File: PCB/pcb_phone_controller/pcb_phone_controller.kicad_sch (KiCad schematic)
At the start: 38 parts, among them SW17 SS-12D00-G 4 E, X1 KAILH-MINI-SILENT-SWITCH, Y1 KAILH-MINI-SILENT-SWITCH

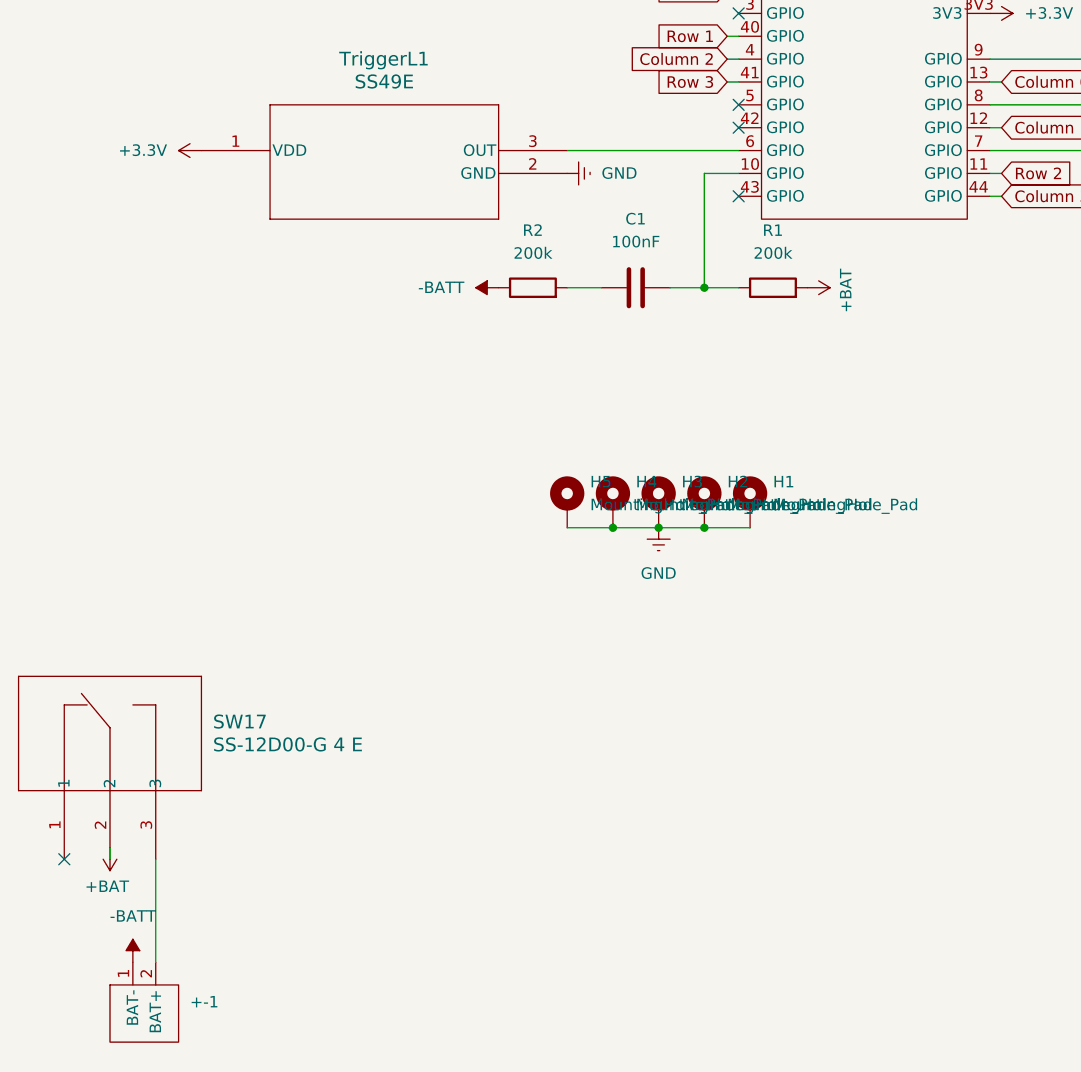
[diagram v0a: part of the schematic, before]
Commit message: Add pads to connect the battery to the µcontroller + add assembly guide
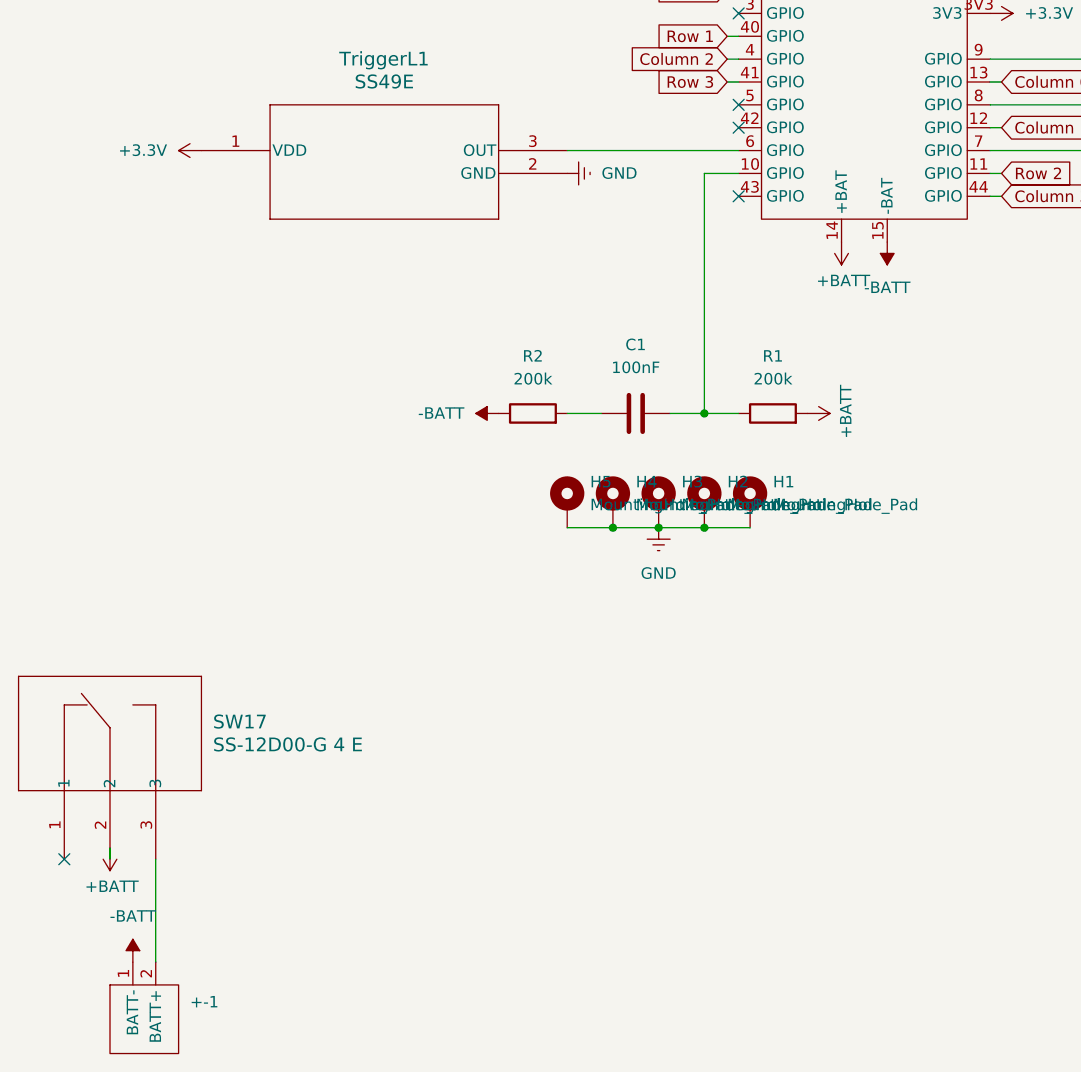
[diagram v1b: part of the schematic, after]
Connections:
- net -BATT: now also U1.15 (-BAT)
- net +BAT renamed +BATT
- net +BATT: now also U1.14 (+BAT)
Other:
- moved on the sheet: +-1, C1, R1, R2
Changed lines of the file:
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@@
 	)
 	(junction
-		(at 109.22 83.82)
+		(at 109.22 97.79)
 		(diameter 0)
 		(color 0 0 0 0)
@@
 	(wire
 		(pts
-			(xy 109.22 71.12) (xy 109.22 83.82)
+			(xy 109.22 71.12) (xy 109.22 97.79)
 		)
 		(stroke
@@
 	(wire
 		(pts
-			(xy 105.41 83.82) (xy 109.22 83.82)
+			(xy 105.41 97.79) (xy 109.22 97.79)
 		)
 		(stroke
@@
 	(wire
 		(pts
-			(xy 93.98 83.82) (xy 97.79 83.82)
+			(xy 93.98 97.79) (xy 97.79 97.79)
 		)
 		(stroke
@@
 	(wire
 		(pts
-			(xy 113.03 83.82) (xy 109.22 83.82)
+			(xy 113.03 97.79) (xy 109.22 97.79)
 		)
 		(stroke
@@
 		(pin "13"
 		)
+		(pin "15"
+		)
+		(pin "14"
+		)
 		(instances
 			(project ""
@@
 	)
 	(symbol
+		(lib_id "power:-BATT")
+		(at 129.54 78.74 180)
+		(unit 1)
+		(exclude_from_sim no)
+		(in_bom yes)
+		(on_board yes)
+		(dnp no)
+		(property "Reference" "#PWR013"
+			(at 129.54 74.93 0)
+			(effects
+				(font
+					(size 1.27 1.27)
+				)
+				(hide yes)
+			)
+		)
+		(property "Value" "-BATT"
+			(at 129.54 83.82 0)
+			(effects
+				(font
+					(size 1.27 1.27)
+				)
+			)
+		)
+		(property "Footprint" ""
+			(at 129.54 78.74 0)
+			(effects
+				(font
+					(size 1.27 1.27)
+				)
+				(hide yes)
+			)
+		)
+		(property "Datasheet" ""
+			(at 129.54 78.74 0)
+			(effects
+				(font
+					(size 1.27 1.27)
+				)
+				(hide yes)
+			)
+		)
+		(property "Description" "Power symbol creates a global label with name \"-BATT\""
+			(at 129.54 78.74 0)
+			(effects
+				(font
+					(size 1.27 1.27)
+				)
+				(hide yes)
+			)
+		)
+		(pin "1"
+		)
+		(instances
+			(project "pcb_phone_controller"
+				(path "/fc840a9c-b1ba-43df-b29f-5e3875a3bf9d"
+					(reference "#PWR013")
+					(unit 1)
+				)
+			)
+		)
+	)
+	(symbol
 		(lib_id "power:Earth")
 		(at 255.27 115.57 0)
@@
 	(symbol
 		(lib_id "Device:C")
-		(at 101.6 83.82 270)
+		(at 101.6 97.79 270)
 		(unit 1)
 		(exclude_from_sim no)
@@
 		(fields_autoplaced yes)
 		(property "Reference" "C1"
-			(at 101.6 76.2 90)
+			(at 101.6 90.17 90)
 			(effects
 				(font
@@
 		)
 		(property "Value" "100nF"
-			(at 101.6 78.74 90)
+			(at 101.6 92.71 90)
 			(effects
 				(font
@@
 		)
 		(property "Footprint" "Capacitor_SMD:C_0805_2012Metric_Pad1.18x1.45mm_HandSolder"
-			(at 97.79 84.7852 0)
+			(at 97.79 98.7552 0)
 			(effects
 				(font
@@
 		)
 		(property "Datasheet" "~"
-			(at 101.6 83.82 0)
+			(at 101.6 97.79 0)
 			(effects
 				(font
@@
 		)
 		(property "Description" "Unpolarized capacitor"
-			(at 101.6 83.82 0)
+			(at 101.6 97.79 0)
 			(effects
 				(font
@@
 	(symbol
 		(lib_id "power:+BATT")
-		(at 120.65 83.82 270)
+		(at 120.65 97.79 270)
 		(unit 1)
 		(exclude_from_sim no)
@@
 		(dnp no)
 		(property "Reference" "#PWR04"
-			(at 116.84 83.82 0)
+			(at 116.84 97.79 0)
 			(effects
 				(font
@@
 			)
 		)
-		(property "Value" "+BAT"
-			(at 124.968 86.614 0)
+		(property "Value" "+BATT"
+			(at 124.968 100.584 0)
 			(effects
 				(font
@@
 		)
 		(property "Footprint" ""
-			(at 120.65 83.82 0)
+			(at 120.65 97.79 0)
 			(effects
 				(font
@@
 		)
 		(property "Datasheet" ""
-			(at 120.65 83.82 0)
+			(at 120.65 97.79 0)
 			(effects
 				(font
@@
 		)
 		(property "Description" "Power symbol creates a global label with name \"+BATT\""
-			(at 120.65 83.82 0)
+			(at 120.65 97.79 0)
 			(effects
 				(font
@@
 			)
 		)
-		(property "Value" "+BAT"
+		(property "Value" "+BATT"
 			(at 40.386 150.368 0)
 			(effects
@@
 	(symbol
 		(lib_id "Device:R")
-		(at 90.17 83.82 90)
+		(at 90.17 97.79 90)
 		(unit 1)
 		(exclude_from_sim no)
@@
 		(fields_autoplaced yes)
 		(property "Reference" "R2"
-			(at 90.17 77.47 90)
+			(at 90.17 91.44 90)
 			(effects
 				(font
@@
 		)
 		(property "Value" "200k"
-			(at 90.17 80.01 90)
+			(at 90.17 93.98 90)
 			(effects
 				(font
@@
 		)
 		(property "Footprint" "Resistor_SMD:R_0805_2012Metric_Pad1.20x1.40mm_HandSolder"
-			(at 90.17 85.598 90)
+			(at 90.17 99.568 90)
 			(effects
 				(font
@@
 		)
 		(property "Datasheet" "~"
-			(at 90.17 83.82 0)
+			(at 90.17 97.79 0)
 			(effects
 				(font
@@
 		)
 		(property "Description" "Resistor"
-			(at 90.17 83.82 0)
+			(at 90.17 97.79 0)
 			(effects
 				(font
@@
 	(symbol
 		(lib_id "Device:R")
-		(at 116.84 83.82 90)
+		(at 116.84 97.79 90)
 		(unit 1)
 		(exclude_from_sim no)
@@
 		(fields_autoplaced yes)
 		(property "Reference" "R1"
-			(at 116.84 77.47 90)
+			(at 116.84 91.44 90)
 			(effects
 				(font
@@
 		)
 		(property "Value" "200k"
-			(at 116.84 80.01 90)
+			(at 116.84 93.98 90)
 			(effects
 				(font
@@
 		)
 		(property "Footprint" "Resistor_SMD:R_0805_2012Metric_Pad1.20x1.40mm_HandSolder"
-			(at 116.84 85.598 90)
+			(at 116.84 99.568 90)
 			(effects
 				(font
@@
 		)
 		(property "Datasheet" "~"
-			(at 116.84 83.82 0)
+			(at 116.84 97.79 0)
 			(effects
 				(font
@@
 		)
 		(property "Description" "Resistor"
-			(at 116.84 83.82 0)
+			(at 116.84 97.79 0)
 			(effects
 				(font
@@
 	(symbol
 		(lib_id "power:-BATT")
-		(at 86.36 83.82 90)
+		(at 86.36 97.79 90)
 		(unit 1)
 		(exclude_from_sim no)
@@
 		(fields_autoplaced yes)
 		(property "Reference" "#PWR05"
-			(at 90.17 83.82 0)
+			(at 90.17 97.79 0)
 			(effects
 				(font
@@
 		)
 		(property "Value" "-BATT"
-			(at 82.55 83.8199 90)
+			(at 82.55 97.7899 90)
 			(effects
 				(font
@@
 		)
 		(property "Footprint" ""
-			(at 86.36 83.82 0)
+			(at 86.36 97.79 0)
 			(effects
 				(font
@@
 		)
 		(property "Datasheet" ""
-			(at 86.36 83.82 0)
+			(at 86.36 97.79 0)
 			(effects
 				(font
@@
 			)
 		)
-		(property "Description" "Power symbol creates a global label with name \"-BATT\""
-			(at 86.36 83.82 0)
+		(property "Description" "Power symbol creates a global label with name \"-BAT\""
+			(at 86.36 97.79 0)
+			(effects
+				(font
+					(size 1.27 1.27)
+				)
+				(hide yes)
+			)
+		)
+		(property "Field5" ""
+			(at 86.36 97.79 0)
 			(effects
 				(font
@@
 					(unit 1)
 				)
+			)
+		)
+	)
+	(symbol
+		(lib_id "power:+BATT")
+		(at 124.46 78.74 180)
+		(unit 1)
+		(exclude_from_sim no)
+		(in_bom yes)
+		(on_board yes)
+		(dnp no)
+		(property "Reference" "#PWR03"
+			(at 124.46 74.93 0)
+			(effects
+				(font
+					(size 1.27 1.27)
+				)
+				(hide yes)
+			)
+		)
+		(property "Value" "+BATT"
+			(at 121.666 83.058 0)
+			(effects
+				(font
+					(size 1.27 1.27)
+				)
+				(justify right)
+			)
+		)
+		(property "Footprint" ""
+			(at 124.46 78.74 0)
+			(effects
+				(font
+					(size 1.27 1.27)
+				)
+				(hide yes)
+			)
+		)
+		(property "Datasheet" ""
+			(at 124.46 78.74 0)
+			(effects
+				(font
+					(size 1.27 1.27)
+				)
+				(hide yes)
+			)
+		)
+		(property "Description" "Power symbol creates a global label with name \"+BATT\""
+			(at 124.46 78.74 0)
+			(effects
+				(font
+					(size 1.27 1.27)
+				)
+				(hide yes)
+			)
+		)
+		(pin "1"
+		)
+		(instances
+			(project "pcb_phone_controller"
+				(path "/fc840a9c-b1ba-43df-b29f-5e3875a3bf9d"
+					(reference "#PWR03")
+					(unit 1)
+				)

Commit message: Add a 3D model for the TTP223
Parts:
- BumperL1, BumperR1, ClickStickL1, ClickStickR1: footprint Lib_controller:PinHeader_1x03_P2.54mm_Vertical -> Lib_controller:TTP223
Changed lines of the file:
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@@
 			)
 		)
-		(property "Footprint" "Lib_controller:PinHeader_1x03_P2.54mm_Vertical"
+		(property "Footprint" "Lib_controller:TTP223"
 			(at 213.36 105.41 0)
 			(effects
@@
 			)
 		)
-		(property "Footprint" "Lib_controller:PinHeader_1x03_P2.54mm_Vertical"
+		(property "Footprint" "Lib_controller:TTP223"
 			(at 236.22 105.41 0)
 			(effects
@@
 			)
 		)
-		(property "Footprint" "Lib_controller:PinHeader_1x03_P2.54mm_Vertical"
+		(property "Footprint" "Lib_controller:TTP223"
 			(at 252.73 105.41 0)
 			(effects
@@
 			)
 		)
-		(property "Footprint" "Lib_controller:PinHeader_1x03_P2.54mm_Vertical"
+		(property "Footprint" "Lib_controller:TTP223"
 			(at 275.59 105.41 0)
 			(effects

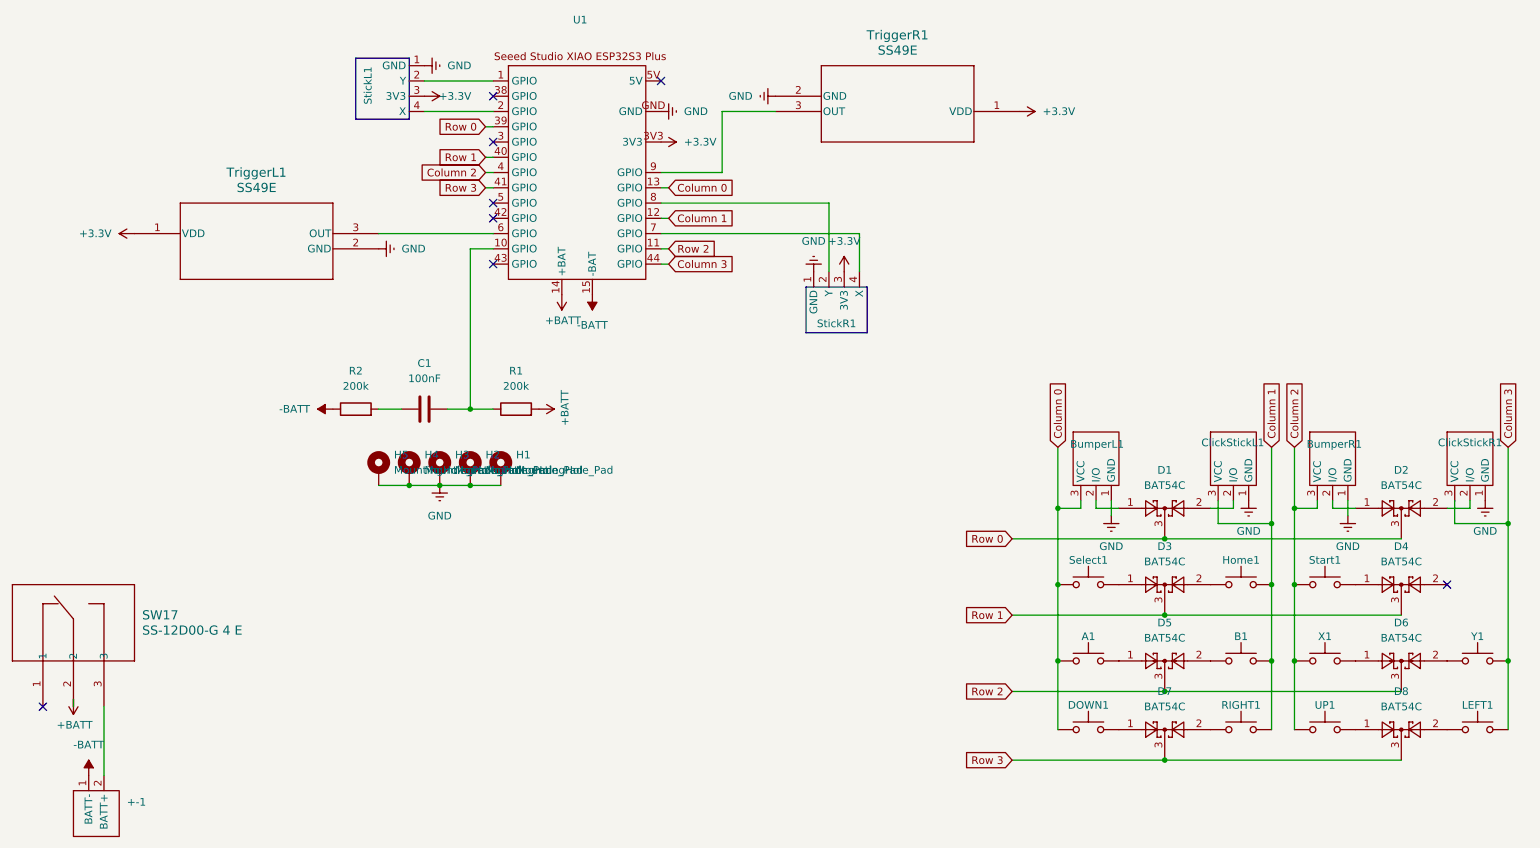
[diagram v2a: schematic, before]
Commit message: Change capacitives buttons to digitals ones and add real pullup
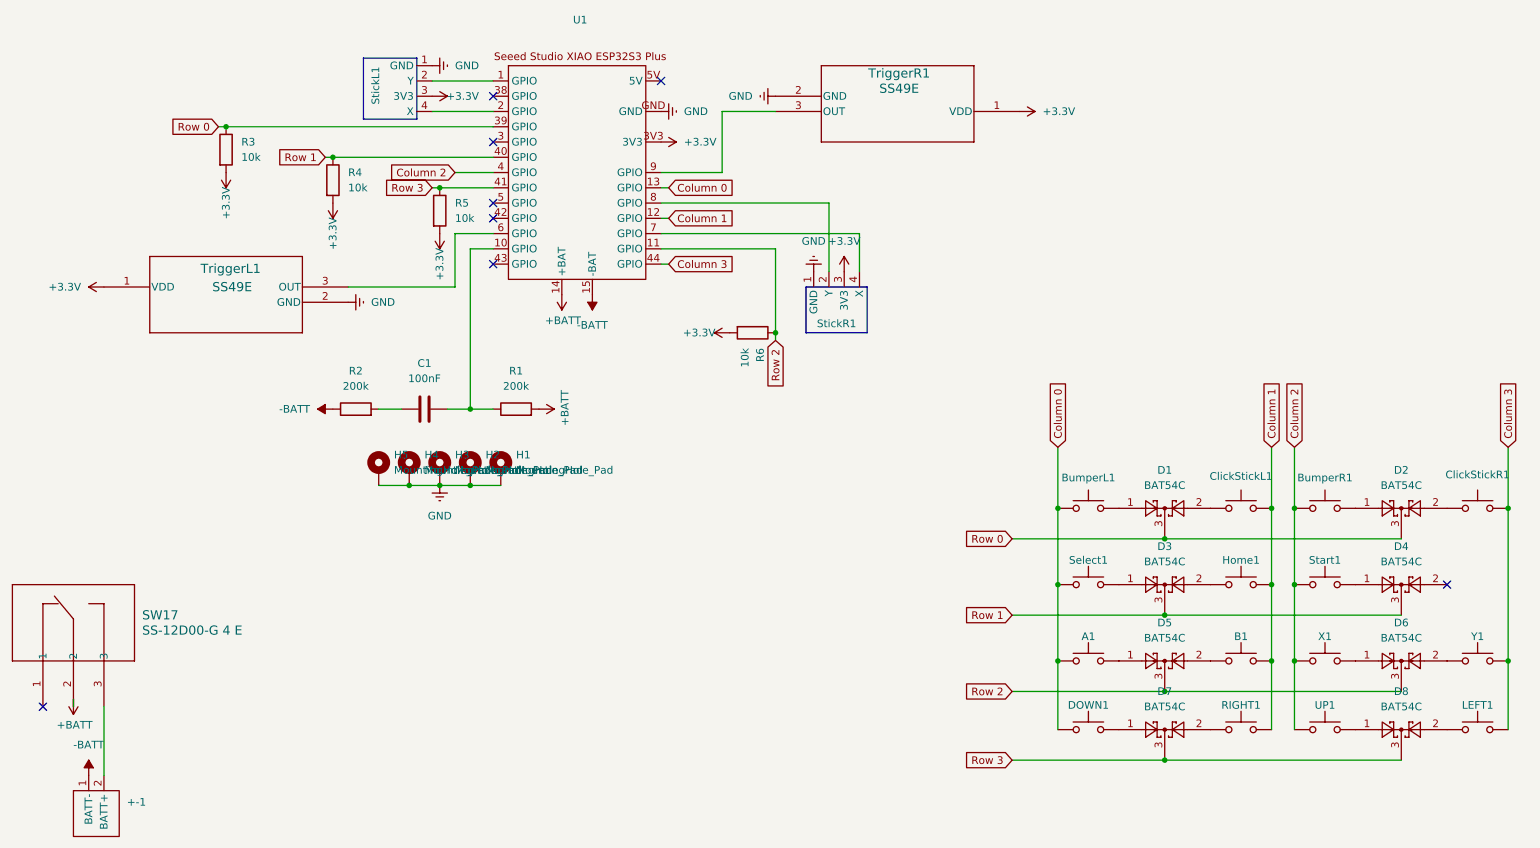
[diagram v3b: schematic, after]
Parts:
- removed BumperL1, BumperR1, ClickStickL1, ClickStickR1: ~, Lib_controller:TTP223, symbol Lib_controller:Capacitive_touch_sensor
- added BumperL1, BumperR1, ClickStickL1, ClickStickR1: Thin membrane button, Lib_controller:SKRWADE030, symbol Lib_controller:Membrane_button
- added R3, R4, R5, R6: 10k, Resistor_SMD:R_0805_2012Metric_Pad1.20x1.40mm_HandSolder, symbol Device:R
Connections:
- net +3.3V: now also R3.2, R4.2, R5.2, R6.2
- net Column 0: now also BumperL1.1
- net Column 1: now also ClickStickL1.2
- net Column 2: now also BumperR1.1
- net Column 3: now also ClickStickR1.2
- net Row 0: now also R3.1
- net Row 1: now also R4.1
- net Row 2: now also R6.1
- net Row 3: now also R5.1
- net at D1.1: now also BumperL1.2
- net at D1.2: now also ClickStickL1.1
- net at D2.1: now also BumperR1.2
- net at D2.2: now also ClickStickR1.1
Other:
- moved on the sheet: StickL1, TriggerL1
